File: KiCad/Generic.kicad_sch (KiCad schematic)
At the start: 35 parts, among them J1 Connector, J2 USB-C, J3 DC, U1 ESP32-WROOM-32, U2 FT231XQ, U4 LMR16006+FB

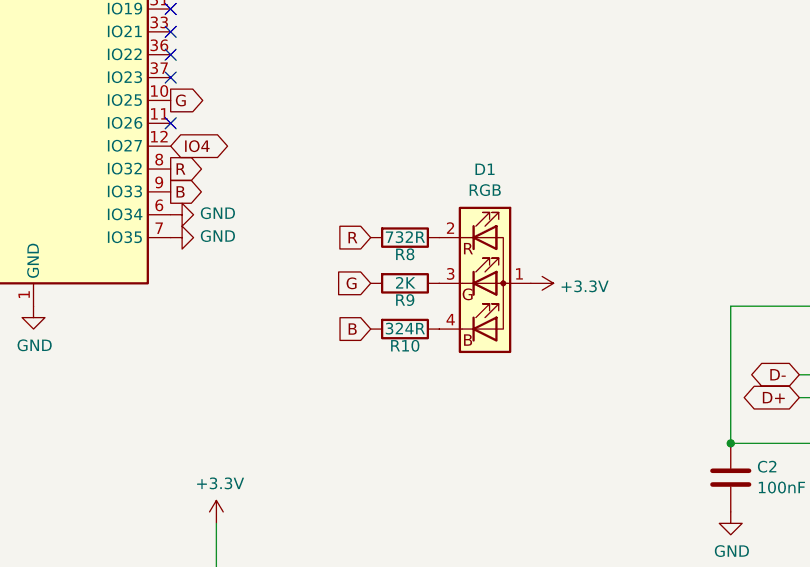
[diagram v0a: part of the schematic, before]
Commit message: Change res values for LED
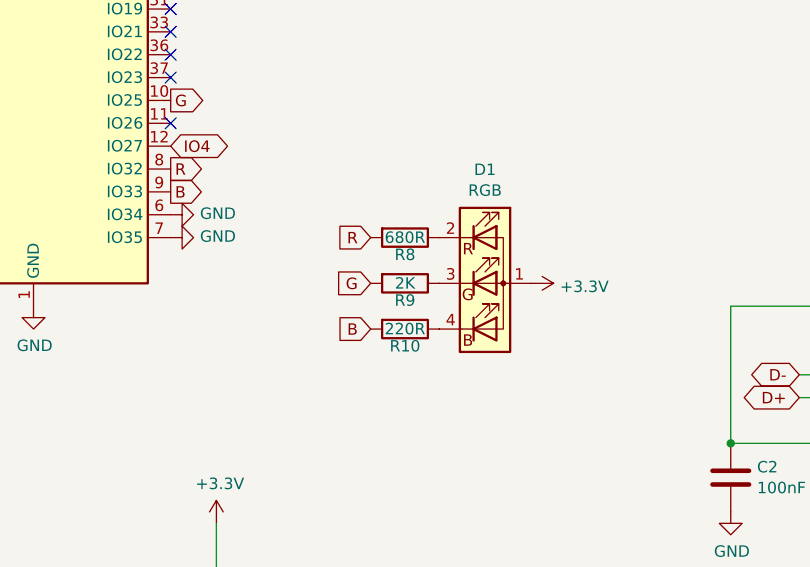
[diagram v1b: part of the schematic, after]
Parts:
- R10: value 324R -> 220R
- R8: value 732R -> 680R
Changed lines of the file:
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@@
     (in_bom yes) (on_board yes)
     (property "Reference" "R10" (id 0) (at 106.68 107.315 90))
-    (property "Value" "324R" (id 1) (at 106.68 105.41 90))
+    (property "Value" "220R" (id 1) (at 106.68 105.41 90))
     (property "Footprint" "RevK:R_0603" (id 2) (at 106.68 103.632 90)
       (effects (font (size 1.27 1.27)) hide)
@@
     (in_bom yes) (on_board yes)
     (property "Reference" "R8" (id 0) (at 106.68 97.155 90))
-    (property "Value" "732R" (id 1) (at 106.68 95.25 90))
+    (property "Value" "680R" (id 1) (at 106.68 95.25 90))
     (property "Footprint" "RevK:R_0603" (id 2) (at 106.68 93.472 90)
       (effects (font (size 1.27 1.27)) hide)
@@
     )
     (path "/00000000-0000-0000-0000-000060cf9e4d"
-      (reference "R8") (unit 1) (value "732R") (footprint "RevK:R_0603")
+      (reference "R8") (unit 1) (value "680R") (footprint "RevK:R_0603")
     )
     (path "/00000000-0000-0000-0000-000060cfbfaf"
@@
     )
     (path "/00000000-0000-0000-0000-000060a436c8"
-      (reference "R10") (unit 1) (value "324R") (footprint "RevK:R_0603")
+      (reference "R10") (unit 1) (value "220R") (footprint "RevK:R_0603")
     )
     (path "/00000000-0000-0000-0000-00006043a8ad"

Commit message: New bigger generic and tidy library
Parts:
- C1, R2, R3, R4, R5, R6, R7: footprint RevK:Pad_1206_0805_NF -> RevK:Pad_1206_0805_Open; now left out of the parts list
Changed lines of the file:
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@@
   )
   (symbol (lib_id "Device:R") (at 83.185 140.97 0) (unit 1)
-    (in_bom yes) (on_board yes)
+    (in_bom no) (on_board yes)
     (property "Reference" "R2" (id 0) (at 84.455 146.05 0)
       (effects (font (size 1.27 1.27)) (justify right))
@@
       (effects (font (size 1.27 1.27)) (justify right))
     )
-    (property "Footprint" "RevK:Pad_1206_0805_NF" (id 2) (at 81.407 140.97 90)
+    (property "Footprint" "RevK:Pad_1206_0805_Open" (id 2) (at 81.407 140.97 90)
       (effects (font (size 1.27 1.27)) hide)
     )
@@
   )
   (symbol (lib_id "Device:R") (at 85.725 140.97 0) (unit 1)
-    (in_bom yes) (on_board yes)
+    (in_bom no) (on_board yes)
     (property "Reference" "R3" (id 0) (at 84.455 146.05 0)
       (effects (font (size 1.27 1.27)) (justify left))
@@
       (effects (font (size 1.27 1.27)) (justify left))
     )
-    (property "Footprint" "RevK:Pad_1206_0805_NF" (id 2) (at 83.947 140.97 90)
+    (property "Footprint" "RevK:Pad_1206_0805_Open" (id 2) (at 83.947 140.97 90)
       (effects (font (size 1.27 1.27)) hide)
     )
@@
   )
   (symbol (lib_id "Device:R") (at 88.265 140.97 0) (unit 1)
-    (in_bom yes) (on_board yes)
+    (in_bom no) (on_board yes)
     (property "Reference" "R4" (id 0) (at 86.995 146.05 0)
       (effects (font (size 1.27 1.27)) (justify left))
@@
       (effects (font (size 1.27 1.27)) (justify left))
     )
-    (property "Footprint" "RevK:Pad_1206_0805_NF" (id 2) (at 86.487 140.97 90)
+    (property "Footprint" "RevK:Pad_1206_0805_Open" (id 2) (at 86.487 140.97 90)
       (effects (font (size 1.27 1.27)) hide)
     )
@@
   )
   (symbol (lib_id "Device:R") (at 90.805 140.97 0) (unit 1)
-    (in_bom yes) (on_board yes)
+    (in_bom no) (on_board yes)
     (property "Reference" "R5" (id 0) (at 89.535 146.05 0)
       (effects (font (size 1.27 1.27)) (justify left))
@@
       (effects (font (size 1.27 1.27)) (justify left))
     )
-    (property "Footprint" "RevK:Pad_1206_0805_NF" (id 2) (at 89.027 140.97 90)
+    (property "Footprint" "RevK:Pad_1206_0805_Open" (id 2) (at 89.027 140.97 90)
       (effects (font (size 1.27 1.27)) hide)
     )
@@
   )
   (symbol (lib_id "Device:R") (at 93.345 140.97 0) (unit 1)
-    (in_bom yes) (on_board yes)
+    (in_bom no) (on_board yes)
     (property "Reference" "R6" (id 0) (at 92.075 146.05 0)
       (effects (font (size 1.27 1.27)) (justify left))
@@
       (effects (font (size 1.27 1.27)) (justify left))
     )
-    (property "Footprint" "RevK:Pad_1206_0805_NF" (id 2) (at 91.567 140.97 90)
+    (property "Footprint" "RevK:Pad_1206_0805_Open" (id 2) (at 91.567 140.97 90)
       (effects (font (size 1.27 1.27)) hide)
     )
@@
   )
   (symbol (lib_id "Device:R") (at 102.235 160.02 270) (unit 1)
-    (in_bom yes) (on_board yes)
+    (in_bom no) (on_board yes)
     (property "Reference" "R7" (id 0) (at 102.235 162.56 90))
     (property "Value" "NF" (id 1) (at 102.235 160.02 90))
-    (property "Footprint" "RevK:Pad_1206_0805_NF" (id 2) (at 102.235 158.242 90)
+    (property "Footprint" "RevK:Pad_1206_0805_Open" (id 2) (at 102.235 158.242 90)
       (effects (font (size 1.27 1.27)) hide)
     )
@@
   )
   (symbol (lib_id "Device:C") (at 74.295 146.05 0) (unit 1)
-    (in_bom yes) (on_board yes)
+    (in_bom no) (on_board yes)
     (property "Reference" "C1" (id 0) (at 74.295 148.59 0)
       (effects (font (size 1.27 1.27)) (justify left))
@@
       (effects (font (size 1.27 1.27)) (justify left))
     )
-    (property "Footprint" "RevK:Pad_1206_0805_NF" (id 2) (at 75.2602 149.86 0)
+    (property "Footprint" "RevK:Pad_1206_0805_Open" (id 2) (at 75.2602 149.86 0)
       (effects (font (size 1.27 1.27)) hide)
     )
@@
     )
     (path "/00000000-0000-0000-0000-000060d24a40"
-      (reference "C1") (unit 1) (value "NF") (footprint "RevK:Pad_1206_0805_NF")
+      (reference "C1") (unit 1) (value "NF") (footprint "RevK:Pad_1206_0805_Open")
     )
     (path "/00000000-0000-0000-0000-0000609259a6"
@@
     )
     (path "/00000000-0000-0000-0000-00006043ffad"
-      (reference "R2") (unit 1) (value "NF") (footprint "RevK:Pad_1206_0805_NF")
+      (reference "R2") (unit 1) (value "NF") (footprint "RevK:Pad_1206_0805_Open")
     )
     (path "/00000000-0000-0000-0000-00006043ffb3"
-      (reference "R3") (unit 1) (value "NF") (footprint "RevK:Pad_1206_0805_NF")
+      (reference "R3") (unit 1) (value "NF") (footprint "RevK:Pad_1206_0805_Open")
     )
     (path "/00000000-0000-0000-0000-00006043ffb9"
-      (reference "R4") (unit 1) (value "NF") (footprint "RevK:Pad_1206_0805_NF")
+      (reference "R4") (unit 1) (value "NF") (footprint "RevK:Pad_1206_0805_Open")
     )
     (path "/00000000-0000-0000-0000-000060d24a3a"
-      (reference "R5") (unit 1) (value "NF") (footprint "RevK:Pad_1206_0805_NF")
+      (reference "R5") (unit 1) (value "NF") (footprint "RevK:Pad_1206_0805_Open")
     )
     (path "/00000000-0000-0000-0000-000060d24a3b"
-      (reference "R6") (unit 1) (value "NF") (footprint "RevK:Pad_1206_0805_NF")
+      (reference "R6") (unit 1) (value "NF") (footprint "RevK:Pad_1206_0805_Open")
     )
     (path "/00000000-0000-0000-0000-000060d24a3f"
-      (reference "R7") (unit 1) (value "NF") (footprint "RevK:Pad_1206_0805_NF")
+      (reference "R7") (unit 1) (value "NF") (footprint "RevK:Pad_1206_0805_Open")
     )
     (path "/00000000-0000-0000-0000-000060cf9e4d"

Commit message: Tidy
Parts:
- added Logo1: AJK, RevK:AJK, symbol RevK:AJK
- renumbered R2 to R1, R11 to R10, R12 to R11, R13 to R12, R14 to R13, R16 to R14, R17 to R15, R3 to R2, R4 to R3, R5 to R4, R6 to R5, R7 to R6, R8 to R7, R9 to R8, R10 to R9, U4 to U3

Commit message: Lots of tidy - mainly silkscreen stuff
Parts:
- J1: footprint RevK:Molex_MiniSPOX_H6RA_0.1 -> RevK:Molex_MiniSPOX_H6RA
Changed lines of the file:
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@@
     (property "Reference" "J1" (id 0) (at 64.3382 142.7226 0))
     (property "Value" "Connector" (id 1) (at 64.3382 145.034 0))
-    (property "Footprint" "RevK:Molex_MiniSPOX_H6RA_0.1" (id 2) (at 61.595 152.4 0)
+    (property "Footprint" "RevK:Molex_MiniSPOX_H6RA" (id 2) (at 61.595 152.4 0)
       (effects (font (size 1.27 1.27)) hide)
     )
@@
     )
     (path "/00000000-0000-0000-0000-000060d24a3c"
-      (reference "J1") (unit 1) (value "Connector") (footprint "RevK:Molex_MiniSPOX_H6RA_0.1")
+      (reference "J1") (unit 1) (value "Connector") (footprint "RevK:Molex_MiniSPOX_H6RA")
     )
     (path "/00000000-0000-0000-0000-000060d24a36"

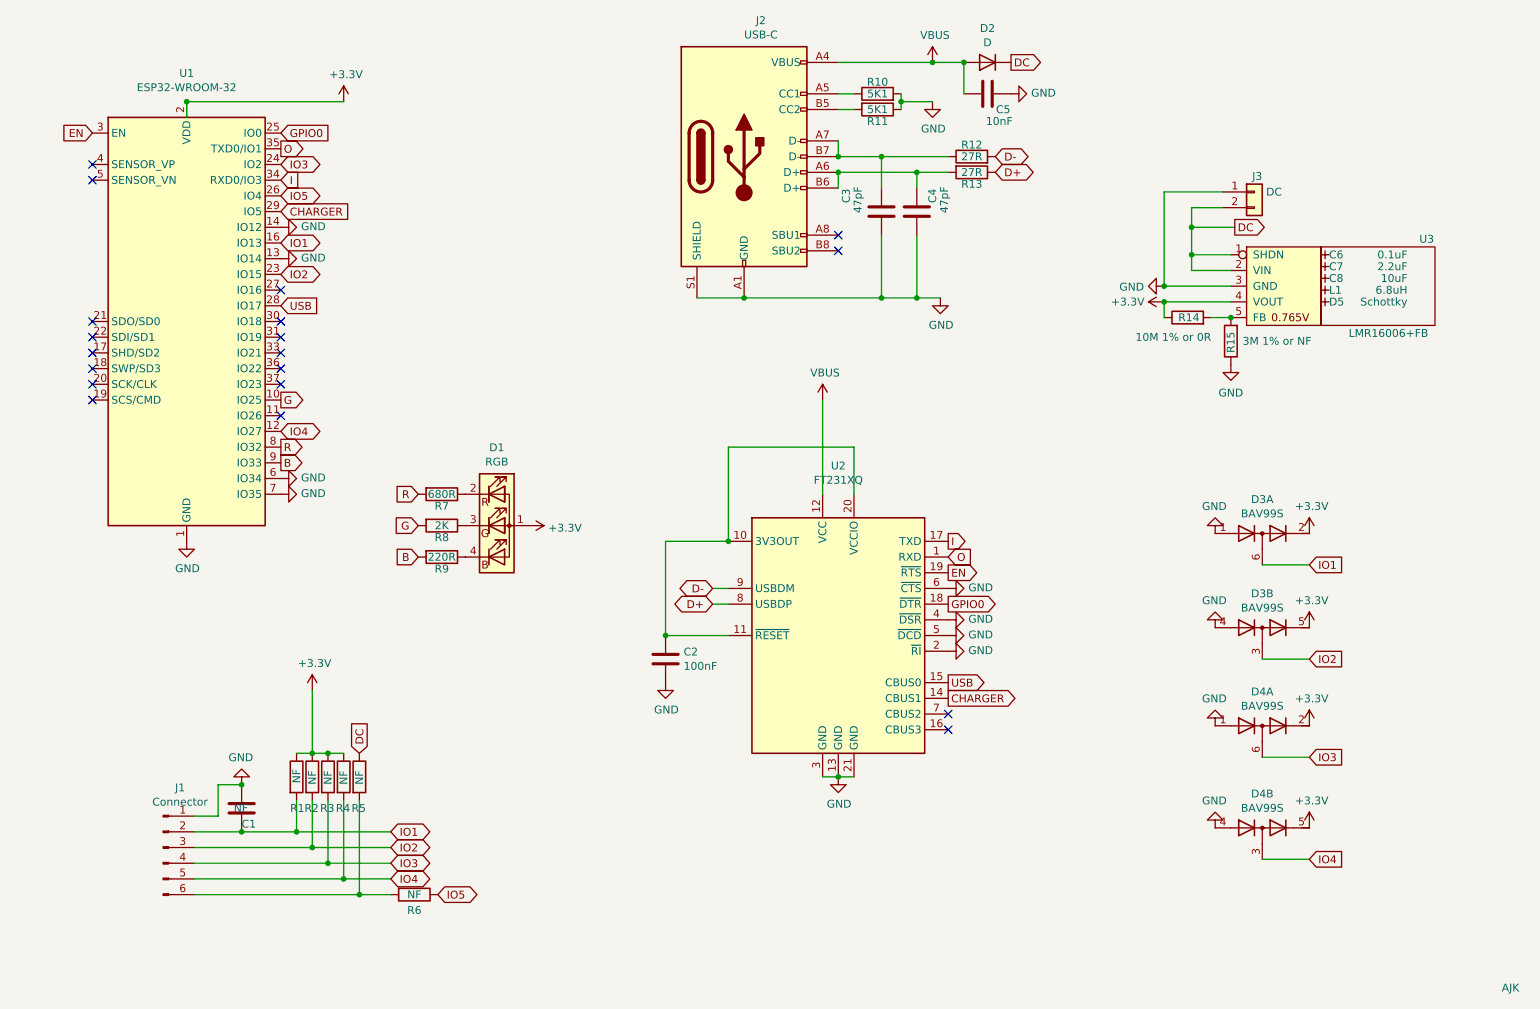
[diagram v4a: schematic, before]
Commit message: Fixed USB/DC stuff on Generic.
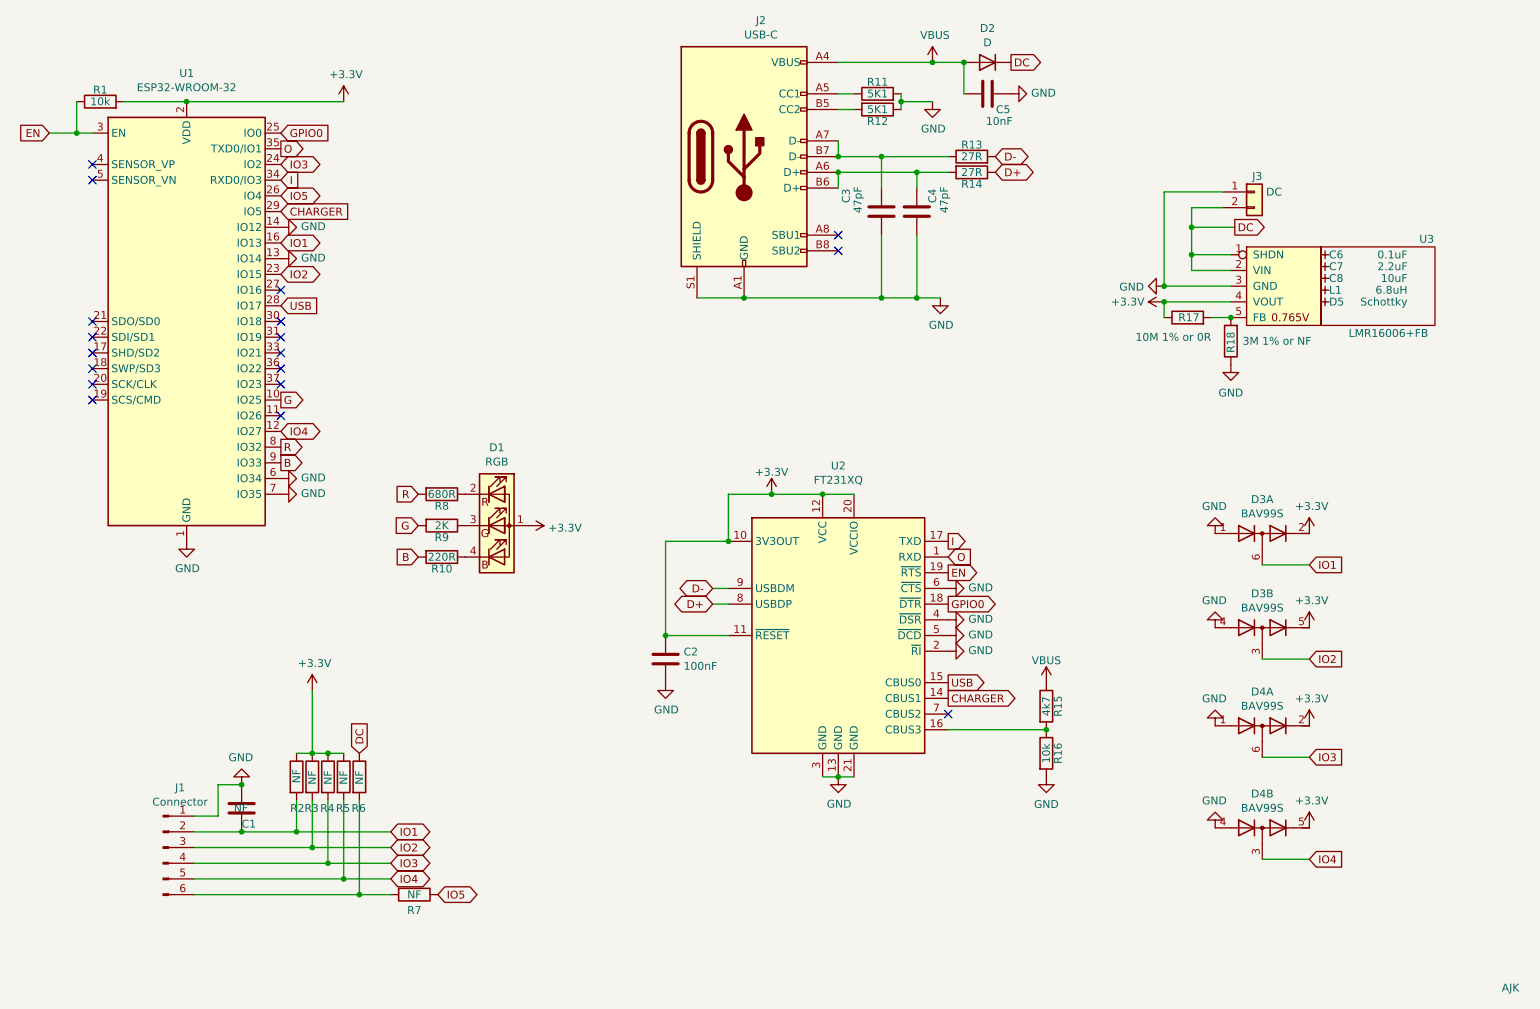
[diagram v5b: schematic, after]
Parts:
- added R1, R16: 10k, RevK:R_0603, symbol Device:R
- added R15: 4k7, RevK:R_0603, symbol Device:R
- renumbered R9 to R10, R10 to R11, R11 to R12, R12 to R13, R13 to R14, R14 to R17, R15 to R18, R1 to R2, R2 to R3, R3 to R4, R4 to R5, R5 to R6, R6 to R7, R7 to R8, R8 to R9
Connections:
- net +3V3: now also C2.1, U2.10 (3V3OUT), U2.11 (~{RESET}), U2.12 (VCC), U2.20 (VCCIO), R1.2
- net EN: now also R1.1
- net GND: now also R16.2
- net VBUS: now also R15.1; no longer U2.12 (VCC)
- net at U2.16 (CBUS3): now also R15.2, R16.1
- no-connect marks 19 -> 18

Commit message: Clean up GPIOs used to avoid clash with strapping at startup
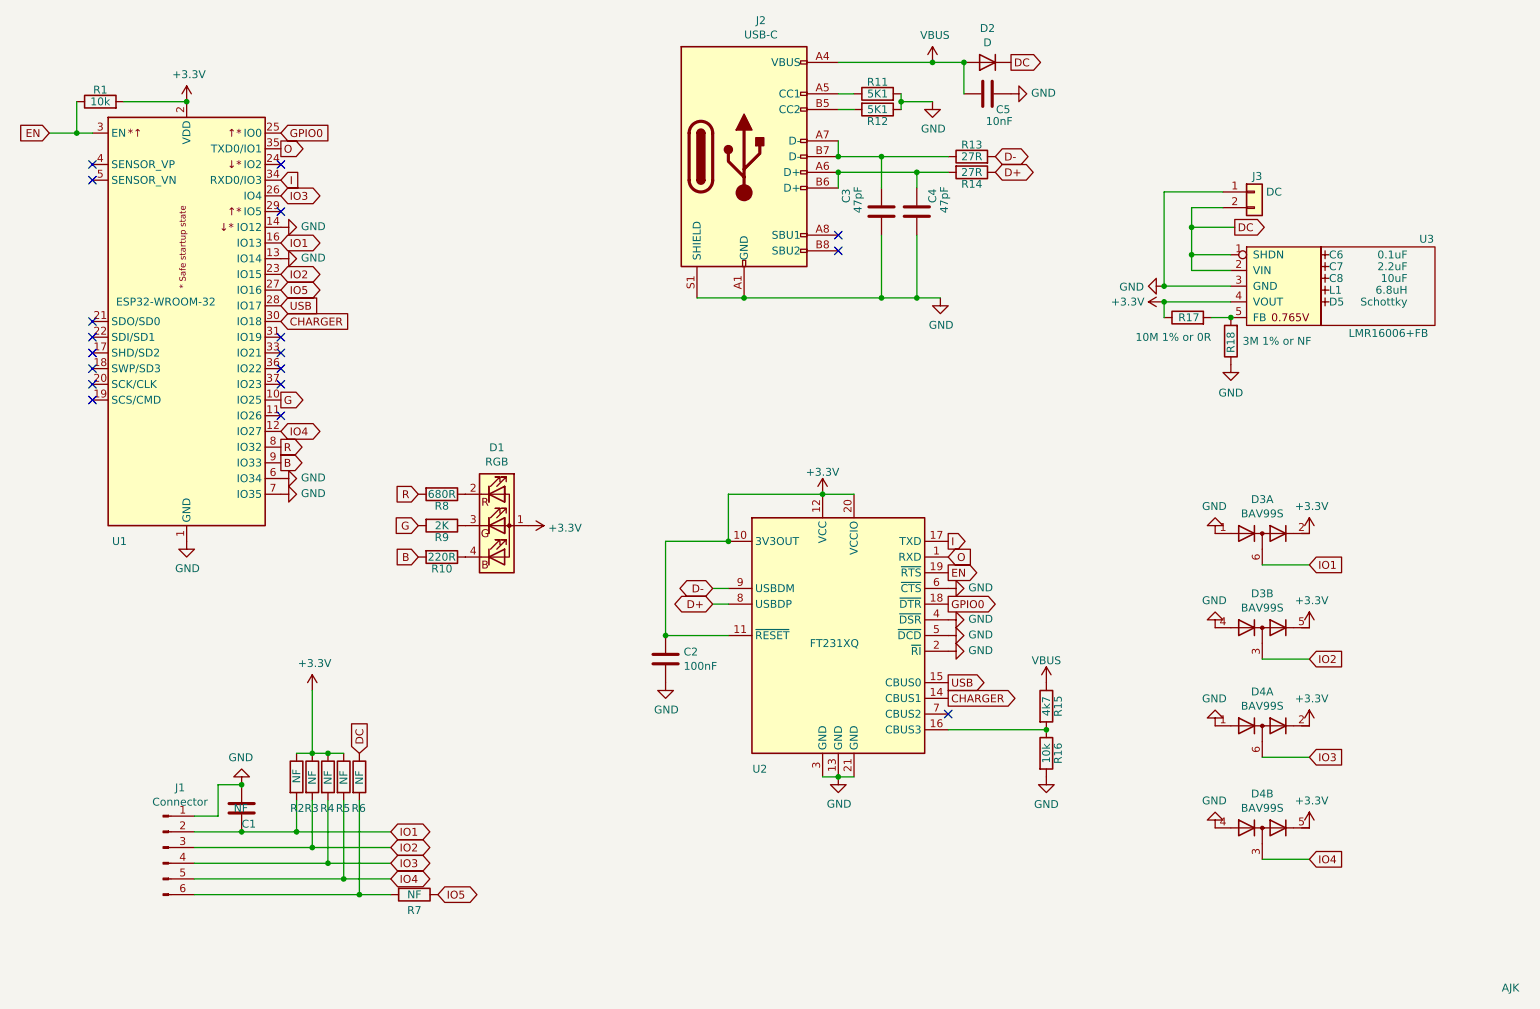
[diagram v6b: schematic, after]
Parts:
- removed U1: ESP32-WROOM-32, RF_Module:ESP32-WROOM-32, symbol RF_Module:ESP32-WROOM-32
- added U1: ESP32-WROOM-32, RF_Module:ESP32-WROOM-32, symbol RevK:ESP32-WROOM-32
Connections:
- net +3V3: now also U1.2 (VDD)
- net B: now also U1.9 (IO33)
- net CHARGER: now also U1.30 (IO18)
- net EN: now also U1.3 (EN)
- net G: now also U1.10 (IO25)
- net GND: now also U1.1 (GND), U1.13 (IO14), U1.14 (IO12), U1.15 (GND), U1.38 (GND), U1.39 (GND), U1.6 (IO34), U1.7 (IO35)
- net GPIO0: now also U1.25 (IO0)
- net I: now also U1.34 (RXD0/IO3)
- net IO1: now also U1.16 (IO13)
- net IO2: now also U1.23 (IO15)
- net IO3: now also U1.26 (IO4)
- net IO4: now also U1.12 (IO27)
- net IO5: now also U1.27 (IO16)
- net O: now also U1.35 (TXD0/IO1)
- net R: now also U1.8 (IO32)
- net USB: now also U1.28 (IO17)
